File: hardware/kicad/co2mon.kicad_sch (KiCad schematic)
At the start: 57 parts, among them J1 SCD30_Conn, J10 TFT_Conn, J11 OLED_Conn, J2 MH_Conn, J3 Z19B_Conn2, J4 T67xx_Conn, J5 Z14A_Conn, J6 Z19B_Conn1, J7 USB_B_Micro, J8 SD_Conn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

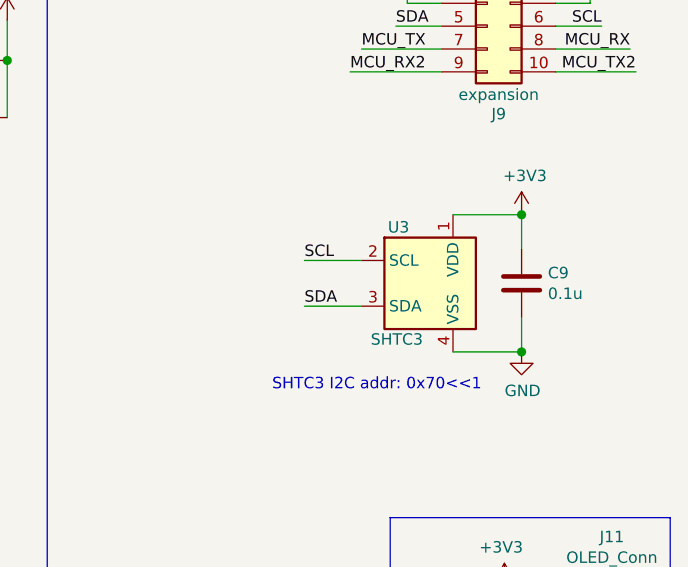
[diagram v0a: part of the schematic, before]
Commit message: remove temp/humidity sensor
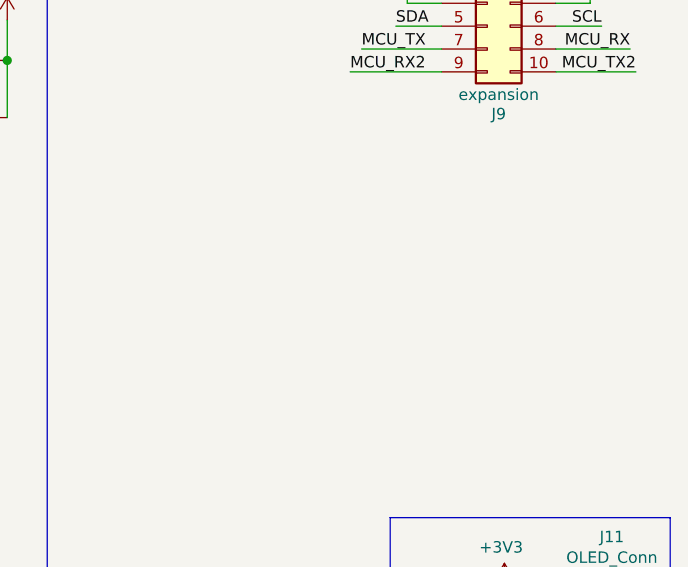
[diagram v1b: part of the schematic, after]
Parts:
- removed C9: 0.1u, Capacitor_SMD:C_0603_1608Metric, symbol Device:C
- removed U3: SHTC3, Sensor_Humidity:Sensirion_DFN-4-1EP_2x2mm_P1mm_EP0.7x1.6mm, symbol Sensor_Humidity:SHTC3
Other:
- note removed: "SHTC3 I2C addr: 0x70<<1"
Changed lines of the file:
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@@
   (junction (at 177.165 156.21) (diameter 1.016) (color 0 0 0 0))
   (junction (at 209.55 31.115) (diameter 1.016) (color 0 0 0 0))
-  (junction (at 266.7 48.26) (diameter 1.016) (color 0 0 0 0))
-  (junction (at 266.7 63.5) (diameter 1.016) (color 0 0 0 0))
   (wire (pts (xy 22.86 42.545) (xy 31.75 42.545))
     (stroke (width 0) (type solid) (color 0 0 0 0))
@@
     (stroke (width 0) (type solid) (color 0 0 0 0))
   )
-  (wire (pts (xy 242.57 53.34) (xy 248.92 53.34))
-    (stroke (width 0) (type solid) (color 0 0 0 0))
-  )
-  (wire (pts (xy 242.57 58.42) (xy 248.92 58.42))
-    (stroke (width 0) (type solid) (color 0 0 0 0))
-  )
   (wire (pts (xy 247.65 32.385) (xy 257.81 32.385))
     (stroke (width 0) (type solid) (color 0 0 0 0))
@@
     (stroke (width 0) (type solid) (color 0 0 0 0))
   )
-  (wire (pts (xy 259.08 48.26) (xy 266.7 48.26))
-    (stroke (width 0) (type solid) (color 0 0 0 0))
-  )
-  (wire (pts (xy 259.08 63.5) (xy 266.7 63.5))
-    (stroke (width 0) (type solid) (color 0 0 0 0))
-  )
   (wire (pts (xy 264.795 89.535) (xy 273.685 89.535))
     (stroke (width 0) (type solid) (color 0 0 0 0))
@@
   )
   (wire (pts (xy 266.065 120.65) (xy 266.065 118.745))
-    (stroke (width 0) (type solid) (color 0 0 0 0))
-  )
-  (wire (pts (xy 266.7 48.26) (xy 266.7 52.07))
-    (stroke (width 0) (type solid) (color 0 0 0 0))
-  )
-  (wire (pts (xy 266.7 59.69) (xy 266.7 63.5))
     (stroke (width 0) (type solid) (color 0 0 0 0))
   )
@@
     (effects (font (size 1.27 1.27)) (justify right bottom))
   )
-  (text "SHTC3 I2C addr: 0x70<<1" (at 262.255 67.945 180)
-    (effects (font (size 1.27 1.27)) (justify right bottom))
-  )
   (text "SSD1306 I2C addr: 0x3c<<1\nOLED 128x64\nDisplay Option 2"
     (at 281.94 106.045 0)
@@
     (effects (font (size 1.27 1.27)) (justify right bottom))
   )
-  (label "SCL" (at 242.57 53.34 0)
-    (effects (font (size 1.27 1.27)) (justify left bottom))
-  )
-  (label "SDA" (at 242.57 58.42 0)
-    (effects (font (size 1.27 1.27)) (justify left bottom))
-  )
   (label "MCU_RX2" (at 247.65 32.385 0)
     (effects (font (size 1.27 1.27)) (justify left bottom))
@@
     )
   )
-  (symbol (lib_id "power:+3V3") (at 266.7 48.26 0) (unit 1)
-    (in_bom yes) (on_board yes)
-    (property "Reference" "#PWR053" (id 0) (at 266.7 52.07 0)
-      (effects (font (size 1.27 1.27)) hide)
-    )
-    (property "Value" "+3V3" (id 1) (at 267.0683 43.9356 0))
-    (property "Footprint" "" (id 2) (at 266.7 48.26 0)
-      (effects (font (size 1.27 1.27)) hide)
-    )
-    (property "Datasheet" "" (id 3) (at 266.7 48.26 0)
-      (effects (font (size 1.27 1.27)) hide)
-    )
-  )
   (symbol (lib_id "power:+3V3") (at 267.97 116.84 0) (mirror y) (unit 1)
     (in_bom yes) (on_board yes)
@@
     )
     (property "Datasheet" "" (id 3) (at 264.795 92.075 0)
-      (effects (font (size 1.27 1.27)) hide)
-    )
-  )
-  (symbol (lib_id "power:GND") (at 266.7 63.5 0) (unit 1)
-    (in_bom yes) (on_board yes)
-    (property "Reference" "#PWR054" (id 0) (at 266.7 69.85 0)
-      (effects (font (size 1.27 1.27)) hide)
-    )
-    (property "Value" "GND" (id 1) (at 266.8143 67.8244 0))
-    (property "Footprint" "" (id 2) (at 266.7 63.5 0)
-      (effects (font (size 1.27 1.27)) hide)
-    )
-    (property "Datasheet" "" (id 3) (at 266.7 63.5 0)
       (effects (font (size 1.27 1.27)) hide)
     )
@@
     )
     (property "Datasheet" "~" (id 3) (at 171.45 26.67 0)
-      (effects (font (size 1.27 1.27)) hide)
-    )
-  )
-  (symbol (lib_id "Device:C") (at 266.7 55.88 180) (unit 1)
-    (in_bom yes) (on_board yes)
-    (property "Reference" "C9" (id 0) (at 269.6211 54.7306 0)
-      (effects (font (size 1.27 1.27)) (justify right))
-    )
-    (property "Value" "0.1u" (id 1) (at 269.621 57.029 0)
-      (effects (font (size 1.27 1.27)) (justify right))
-    )
-    (property "Footprint" "Capacitor_SMD:C_0603_1608Metric" (id 2) (at 265.735 52.07 0)
-      (effects (font (size 1.27 1.27)) hide)
-    )
-    (property "Datasheet" "~" (id 3) (at 266.7 55.88 0)
       (effects (font (size 1.27 1.27)) hide)
     )
@@
     )
   )
-  (symbol (lib_id "Sensor_Humidity:SHTC3") (at 256.54 55.88 0) (unit 1)
-    (in_bom yes) (on_board yes)
-    (property "Reference" "U3" (id 0) (at 251.8411 49.6506 0)
-      (effects (font (size 1.27 1.27)) (justify left))
-    )
-    (property "Value" "SHTC3" (id 1) (at 249.9361 62.1093 0)
-      (effects (font (size 1.27 1.27)) (justify left))
-    )
-    (property "Footprint" "Sensor_Humidity:Sensirion_DFN-4-1EP_2x2mm_P1mm_EP0.7x1.6mm" (id 2) (at 261.62 64.77 0)
-      (effects (font (size 1.27 1.27)) hide)
-    )
-    (property "Datasheet" "https://www.sensirion.com/fileadmin/user_upload/customers/sensirion/Dokumente/0_Datasheets/Humidity/Sensirion_Humidity_Sensors_SHTC3_Datasheet.pdf" (id 3) (at 248.92 44.45 0)
-      (effects (font (size 1.27 1.27)) hide)
-    )
-  )
   (symbol (lib_id "Connector:USB_B_Micro") (at 88.265 33.02 0) (unit 1)
     (in_bom yes) (on_board yes)
@@
       (reference "#PWR052") (unit 1) (value "GND") (footprint "")
     )
-    (path "/e008c5ef-a7ff-46b2-8f94-b3ba4addc270"
-      (reference "#PWR053") (unit 1) (value "+3V3") (footprint "")
-    )
-    (path "/a9e4dbe6-bec5-4233-b5df-fc5c32e3cce0"
-      (reference "#PWR054") (unit 1) (value "GND") (footprint "")
-    )
     (path "/d3eaf0e9-86fd-4cfd-b9bc-484f7bc98c03"
       (reference "#PWR055") (unit 1) (value "+3V3") (footprint "")
@@
       (reference "C8") (unit 1) (value "0.1u") (footprint "Capacitor_SMD:C_0603_1608Metric")
     )
-    (path "/114c6cfb-904d-43b6-9c4d-efad4e5f01ab"
-      (reference "C9") (unit 1) (value "0.1u") (footprint "Capacitor_SMD:C_0603_1608Metric")
-    )
     (path "/657fe07a-c55f-4811-b7a3-a0c20367eb38"
       (reference "F1") (unit 1) (value "MICROSMD050F-2") (footprint "Fuse:Fuse_1210_3225Metric")
@@
       (reference "U2") (unit 1) (value "STM32F042K6Tx") (footprint "Package_QFP:LQFP-32_7x7mm_P0.8mm")
     )
-    (path "/bb21c111-8d4f-4a98-9763-53ec6bf1bce4"
-      (reference "U3") (unit 1) (value "SHTC3") (footprint "Sensor_Humidity:Sensirion_DFN-4-1EP_2x2mm_P1mm_EP0.7x1.6mm")
-    )
-  )
+  )
